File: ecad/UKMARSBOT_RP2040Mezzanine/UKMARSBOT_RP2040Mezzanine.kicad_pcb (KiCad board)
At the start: 2 copper layers, 62.5 x 81.3 mm, 17 parts, among them J1 Conn_01x16, J2 Conn_01x06, J3 Conn_01x06, J4 Conn_01x06, J5 Conn_01x04_Pin, SW1 TACT_SW, SW2 TACT_SW, SW3 TACT_SW, U1 Pico

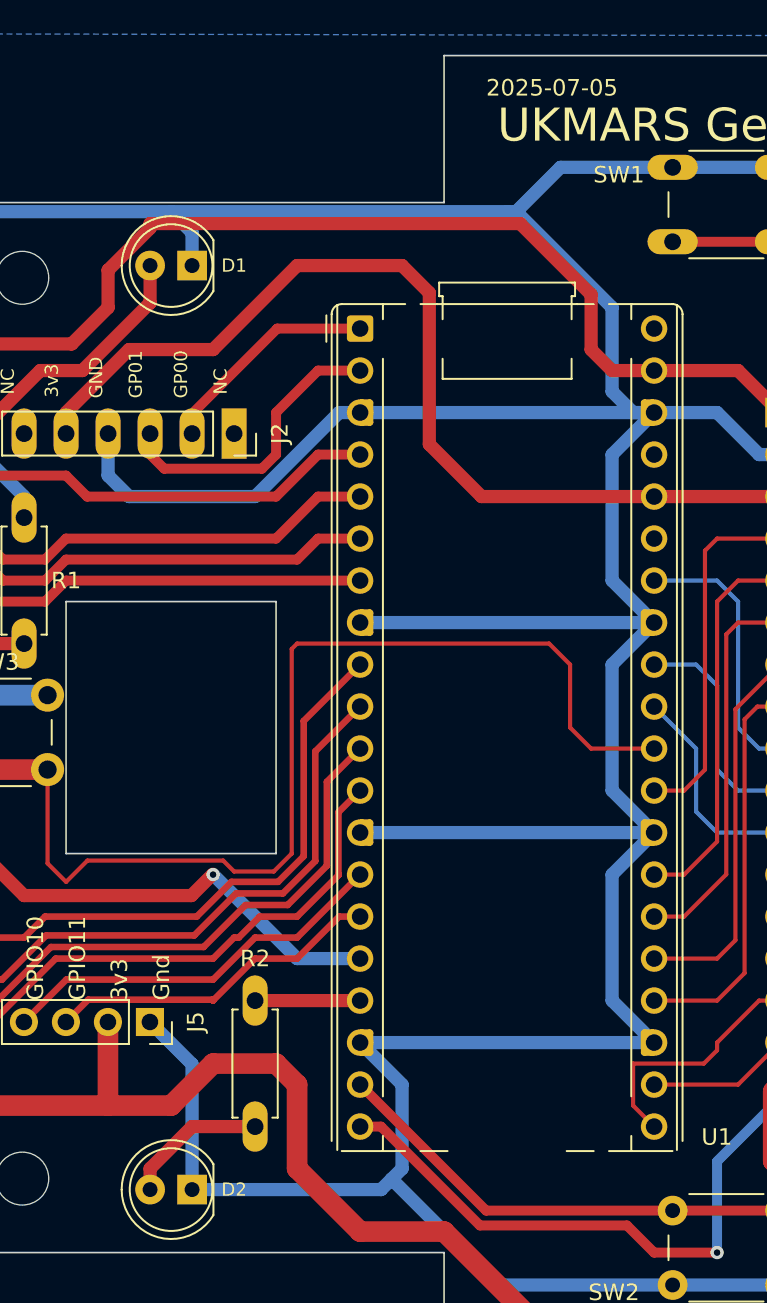
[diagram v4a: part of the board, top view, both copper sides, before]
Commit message: Add v2 wall sensor board
Wall sensor updated for Issues raised on prototype builds. Better pin markings added to Line sensor, mezz and chassis boards
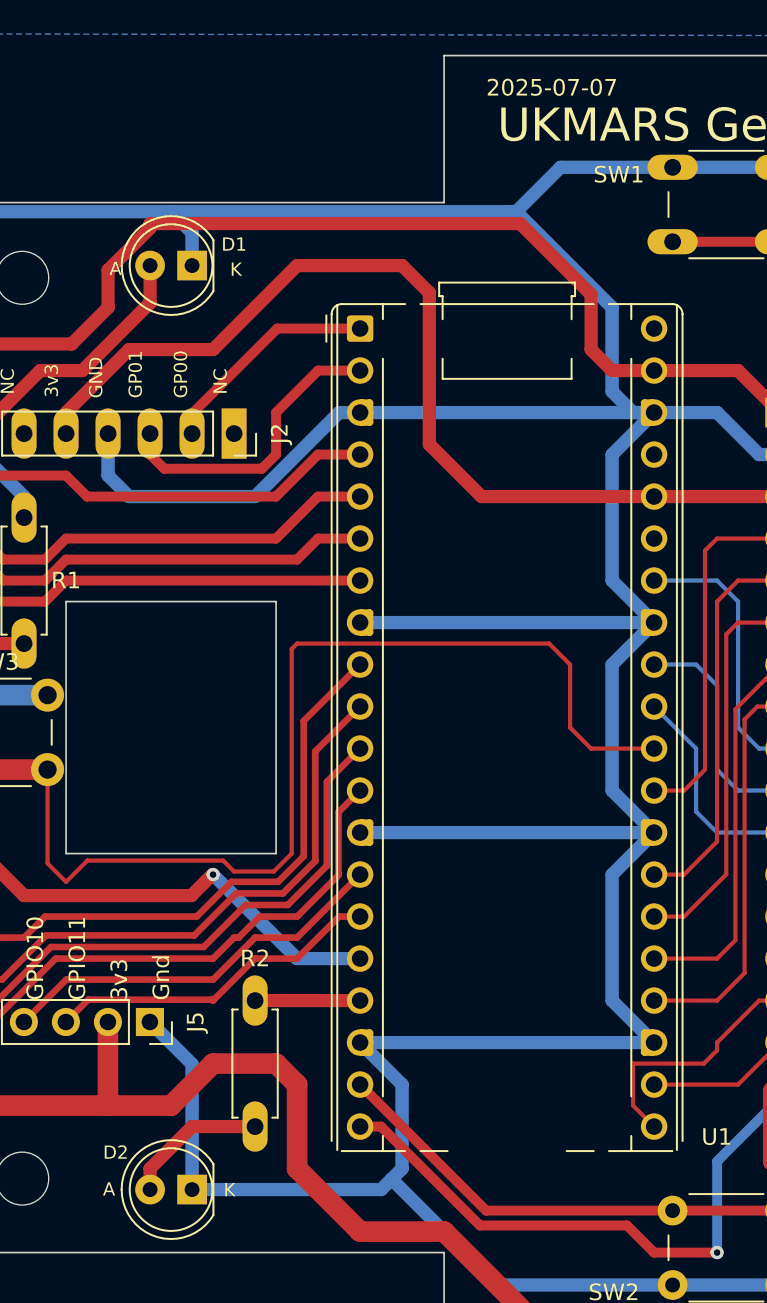
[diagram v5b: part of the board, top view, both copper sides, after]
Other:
- board text added: "2025-07-07"
- board text added: "A"
- board text added: "K"
- board text removed: "2025-07-05"
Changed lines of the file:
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@@
 		(tags "tact sw push 6mm")
 		(property "Reference" "SW3"
-			(at 3.25 -2 360)
+			(at 3.25 -2 0)
 			(layer "F.SilkS")
 			(effects
@@
 		)
 		(property "Value" "TACT_SW"
-			(at 3.75 6.7 360)
+			(at 3.75 6.7 0)
 			(layer "F.Fab")
 			(effects
@@
 		)
 		(fp_text user "${REFERENCE}"
-			(at 3.25 2.25 360)
+			(at 3.25 2.25 0)
 			(layer "F.Fab")
 			(effects
@@
 		(tags "LED")
 		(property "Reference" "D1"
-			(at -2.54 0 0)
+			(at -2.54 1.27 0)
 			(layer "F.SilkS")
 			(effects
@@
 		(tags "LED")
 		(property "Reference" "D2"
-			(at -2.54 0 0)
+			(at 4.6166 2.235948 0)
 			(layer "F.SilkS")
 			(effects
@@
 		(tags "Resistor Axial_DIN0207 series Axial Horizontal pin pitch 7.62mm 0.25W = 1/4W length 6.3mm diameter 2.5mm")
 		(property "Reference" "R2"
-			(at -2.54 0 360)
+			(at -2.54 0 0)
 			(layer "F.SilkS")
 			(effects
@@
 		)
 	)
+	(gr_text "A"
+		(at 116.521551 129.997089 0)
+		(layer "F.SilkS")
+		(effects
+			(font
+				(size 0.8 0.8)
+				(thickness 0.12)
+			)
+			(justify left bottom)
+		)
+	)
 	(gr_text "3v3"
 		(at 159.855527 88.189267 0)
@@
 		)
 	)
+	(gr_text "K"
+		(at 123.818812 130.040525 0)
+		(layer "F.SilkS")
+		(effects
+			(font
+				(size 0.8 0.8)
+				(thickness 0.12)
+			)
+			(justify left bottom)
+		)
+	)
 	(gr_text "A2"
 		(at 159.755527 108.589267 0)
@@
 		)
 	)
-	(gr_text "2025-07-05"
+	(gr_text "2025-07-07"
 		(at 139.7 63.5 0)
 		(layer "F.SilkS")
@@
 		)
 	)
+	(gr_text "K"
+		(at 124.213779 74.375684 0)
+		(layer "F.SilkS")
+		(effects
+			(font
+				(size 0.8 0.8)
+				(thickness 0.12)
+			)
+			(justify left bottom)
+		)
+	)
 	(gr_text "3v3"
 		(at 113.903322 81.63982 90)
@@
 			)
 			(justify left bottom)
+		)
+	)
+	(gr_text "A"
+		(at 116.916518 74.332248 0)
+		(layer "F.SilkS")
+		(effects
+			(font
+				(size 0.8 0.8)
+				(thickness 0.12)
+			)
+			(justify left bottom)

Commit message: V2.1 Boards ready for fabrication
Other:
- board text added: "2.1"
- board text added: "2025-08-16"
- board text removed: "2.0"
- board text removed: "2025-07-07"
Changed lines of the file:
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@@
 		)
 	)
-	(gr_text "2025-07-07"
+	(gr_text "2025-08-16"
 		(at 139.7 63.5 0)
 		(layer "F.SilkS")
@@
 		)
 	)
-	(gr_text "2.0"
+	(gr_text "2.1"
 		(at 163.723173 118.999181 270)
 		(layer "F.SilkS")
